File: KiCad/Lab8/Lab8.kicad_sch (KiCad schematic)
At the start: 37 parts, among them M2 Motor, SW1 Reset, U1 PIC32MX170F256B, U2 74ACT244, U2 SN754410NE, U3 Quadrature_Encoder

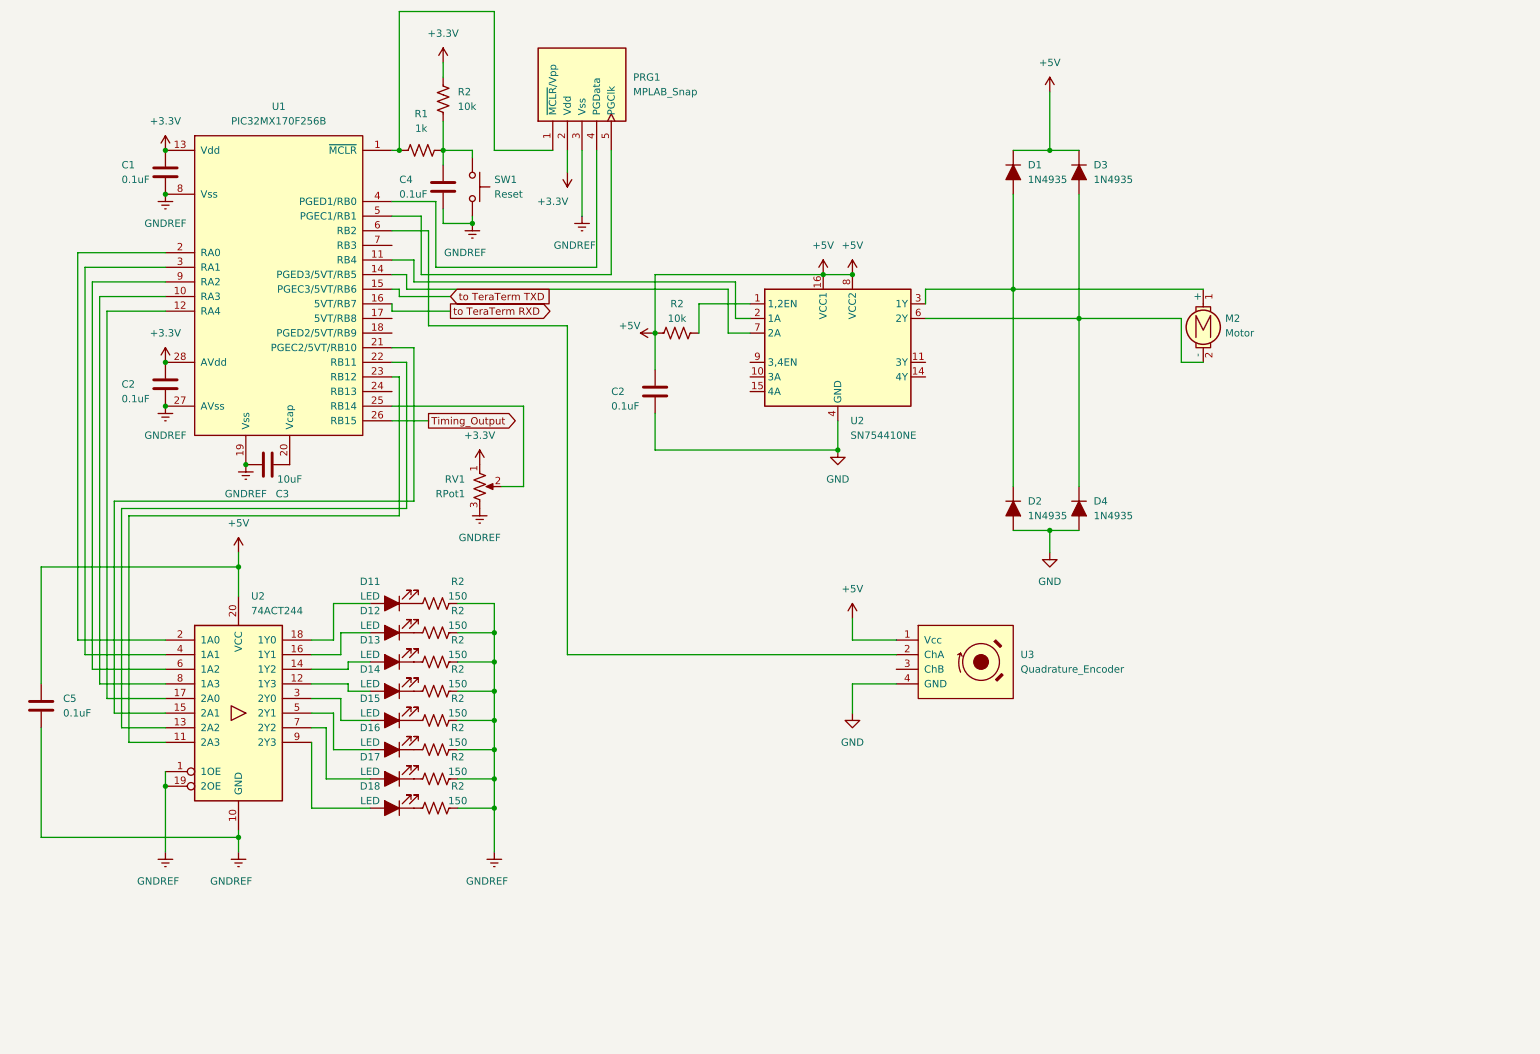
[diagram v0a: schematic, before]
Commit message: Update peoject KiCad schematics
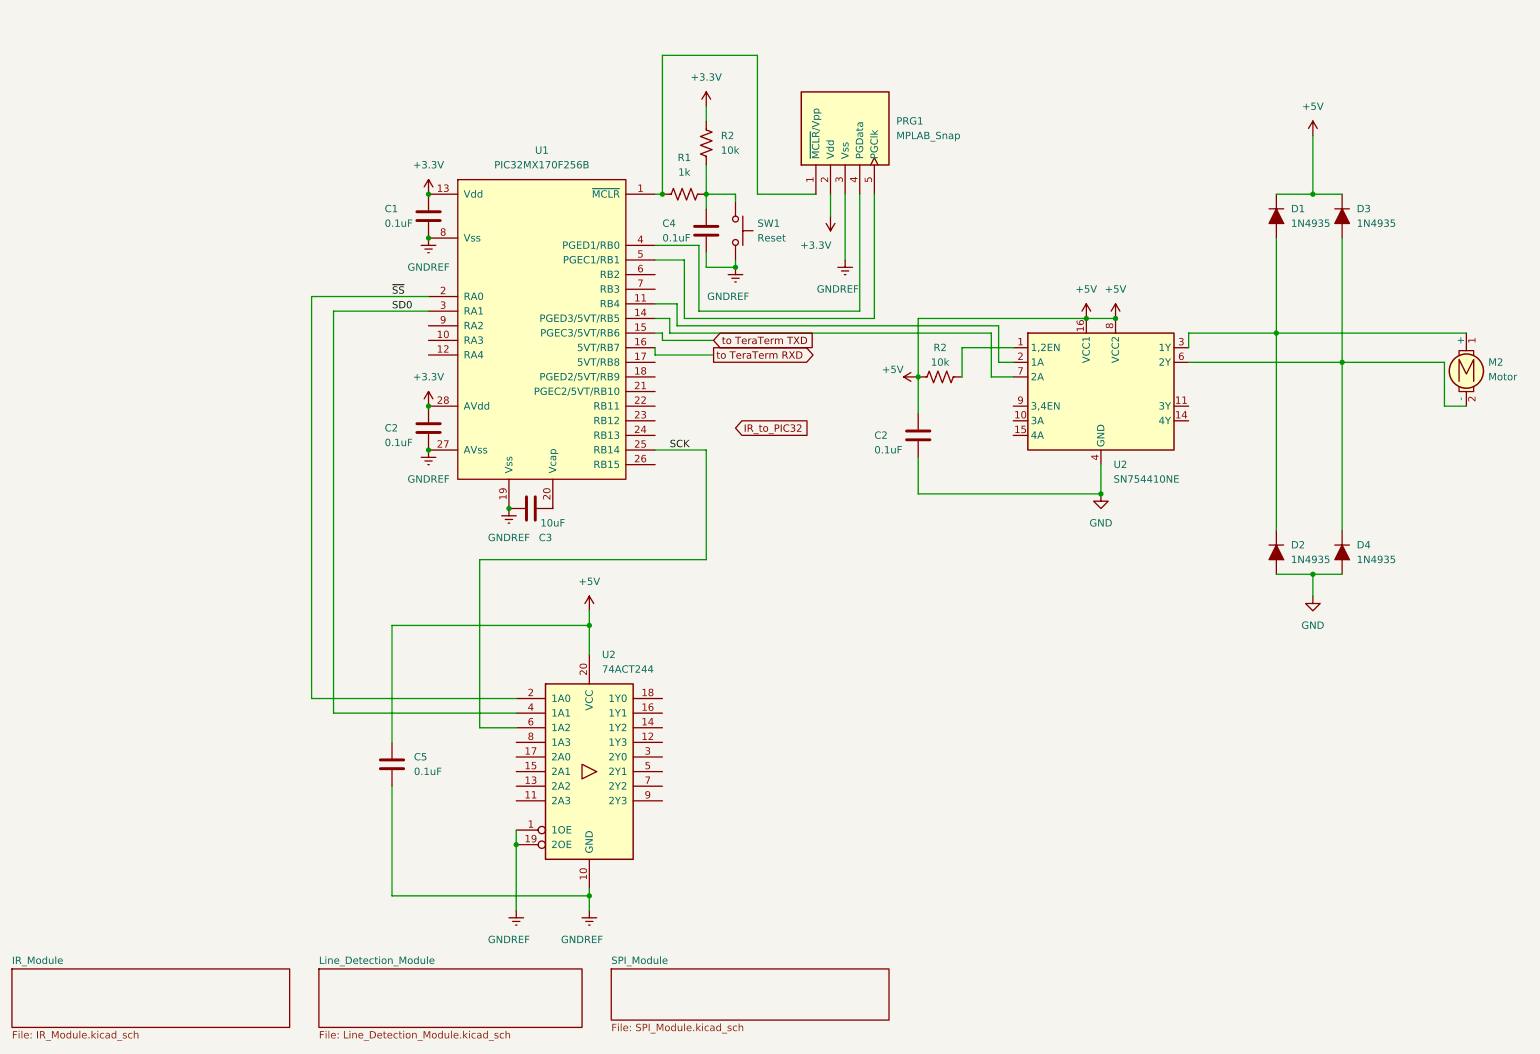
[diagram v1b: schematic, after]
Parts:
- removed D11, D12, D13, D14, D15, D16, D17, D18: LED, symbol ME218_BaseLib:LED
- removed R2 (x8): 150, symbol ME218_BaseLib:Res1
- removed RV1: RPot1, symbol ME218_BaseLib:RPot1
- removed U3: Quadrature_Encoder, symbol ME218_BaseLib:Quadrature_Encoder
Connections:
- net at U1.10 (RA3): no longer U2.8 (1A3)
- net at U1.12 (RA4): no longer U2.17 (2A0)
- net ~{SS}: now reaches U1.2 (RA0), U2.2 (1A0)
- net at U1.21 (PGEC2/5VT/RB10): no longer U2.15 (2A1)
- net at U1.22 (RB11): no longer U2.13 (2A2)
- net at U1.23 (RB12): no longer U2.11 (2A3)
- net SCK: now reaches U1.25 (RB14)
- net SCK: now also U2.6 (1A2)
- net SD0: now reaches U1.3 (RA1), U2.4 (1A1)
- net at U1.9 (RA2): no longer U2.6 (1A2)
- net Timing_Output: no longer names the net of U1.26 (RB15)
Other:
- added sheet IR_Module (IR_Module.kicad_sch)
- added sheet Line_Detection_Module (Line_Detection_Module.kicad_sch)
- added sheet SPI_Module (SPI_Module.kicad_sch)
- moved on the sheet: C1, C2, C3, C4, D1, D2, D3, D4, M2, PRG1, R1, R2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

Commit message: Add in report draft, wire IR in schematics
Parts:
- added D5, D6, D7, D8: 1N4935, symbol ME218_BaseLib:Diode
- added M2: Motor, symbol ME218_BaseLib:Motor
- renumbered M2 to M1
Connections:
- net +5V: now also D5.1 (K), D7.1 (K)
- net GND: now also D6.2 (A), D8.2 (A)
- net IR_to_PIC32: now also U1.6 (RB2)
- net at U1.18 (PGED2/5VT/RB9): now also U2.10 (3A)
- net at U1.24 (RB13): now also U2.15 (4A)
- net at R2.2, U2.1 (1,2EN): now also U2.9 (3,4EN)
- net at U2.11 (3Y): now also D5.2 (A), D6.1 (K), M2.1 (+)
- net at U2.14 (4Y): now also D7.2 (A), D8.1 (K), M2.2 (-)
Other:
- moved on the sheet: C2, D1, D2, D3, D4
